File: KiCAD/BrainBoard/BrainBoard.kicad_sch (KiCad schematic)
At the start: 0 parts

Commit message: [feat] add voltage regulator
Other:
- added sheet Voltage Regulator (voltage_regulator.kicad_sch)
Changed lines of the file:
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@@
 	(generator_version "9.0")
 	(paper "A4")
+	(sheet
+		(at 30.48 66.04)
+		(size 26.67 17.78)
+		(exclude_from_sim no)
+		(in_bom yes)
+		(on_board yes)
+		(dnp no)
+		(fields_autoplaced yes)
+		(stroke
+			(width 0.1524)
+			(type solid)
+		)
+		(fill
+			(color 0 0 0 0.0000)
+		)
+		(property "Sheetname" "Voltage Regulator"
+			(at 30.48 65.3284 0)
+			(effects
+				(font
+					(size 1.27 1.27)
+				)
+				(justify left bottom)
+			)
+		)
+		(property "Sheetfile" "voltage_regulator.kicad_sch"
+			(at 30.48 84.4046 0)
+			(effects
+				(font
+					(size 1.27 1.27)
+				)
+				(justify left top)
+			)
+		)
+		(pin "VOUT" input
+			(at 57.15 74.93 0)
+			(effects
+				(font
+					(size 1.27 1.27)
+				)
+				(justify right)
+			)
+		)
+		(pin "VIN" input
+			(at 30.48 74.93 180)
+			(effects
+				(font
+					(size 1.27 1.27)
+				)
+				(justify left)
+			)
+		)
+		(instances
+			(project "BrainBoard"
+				(path "/44e391a9-9312-4881-bf0a-d93a44472e34"
+					(page "2")
+				)
+			)
+		)
+	)
 	(sheet_instances
 		(path "/"

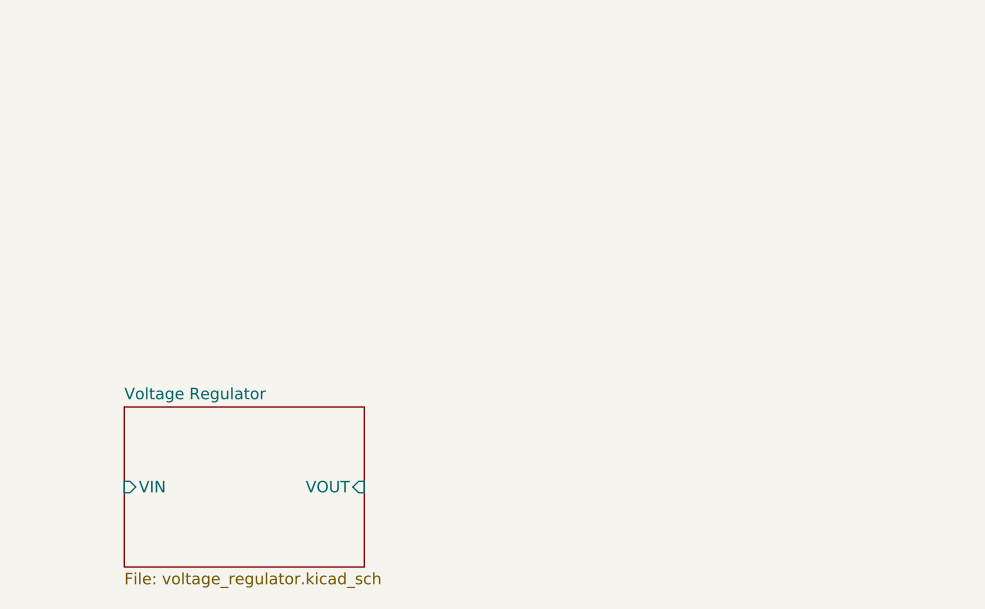
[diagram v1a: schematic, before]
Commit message: [bug] make ERC happy
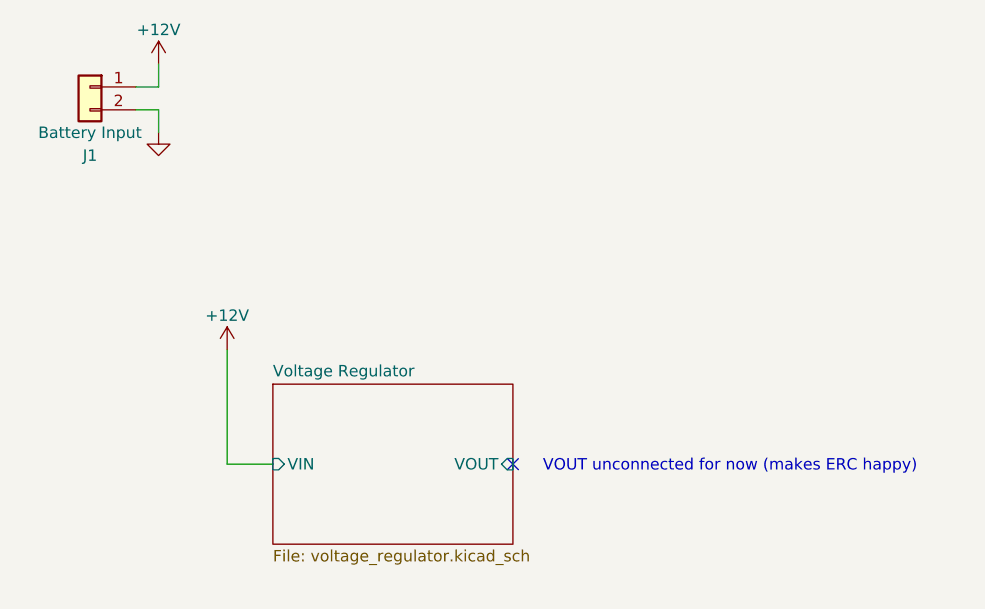
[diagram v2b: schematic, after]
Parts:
- added J1: Battery Input, symbol Connector_Generic:Conn_01x02
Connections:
- new net +12V: J1.1 (Pin_1)
- new net GND: J1.2 (Pin_2)
- no-connect marks 0 -> 1
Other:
- note added: "VOUT unconnected for now (makes ERC happy)"

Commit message: [docs] update page settings
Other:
- company: (none) -> Nathan Wignall, Minh Nguyen, Ana Weiss
- title: (none) -> Ford F150 Raptor SumoBot AL Trim
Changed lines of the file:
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@@
 	(generator_version "9.0")
 	(paper "A4")
+	(title_block
+		(title "Ford F150 Raptor SumoBot AL Trim")
+		(date "${CURRENT_DATE}")
+		(company "Nathan Wignall, Minh Nguyen, Ana Weiss")
+	)
 	(text "VOUT unconnected for now (makes ERC happy)"
 		(exclude_from_sim no)
